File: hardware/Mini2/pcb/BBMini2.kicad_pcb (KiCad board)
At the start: 4 copper layers, 88 x 50 mm, 79 parts, among them J1 Conn_01x02, J2 USB_B_Mini, Q1 MBT2222ADW1T1, SW1 SW_SPDT, SW2 SW_Push, SW3 SW_Push, SW4 SW_Push, U1 ESP8266EX, U2 AT25SF081-SSHF-X, U3 AP2112K-3.3, U4 CP2104, U5 MCP3208, U6 LM2576S-5, U7 HD44780, U8 74HC595, Y1 ABM8-26.000MHZ-10-1-U-T

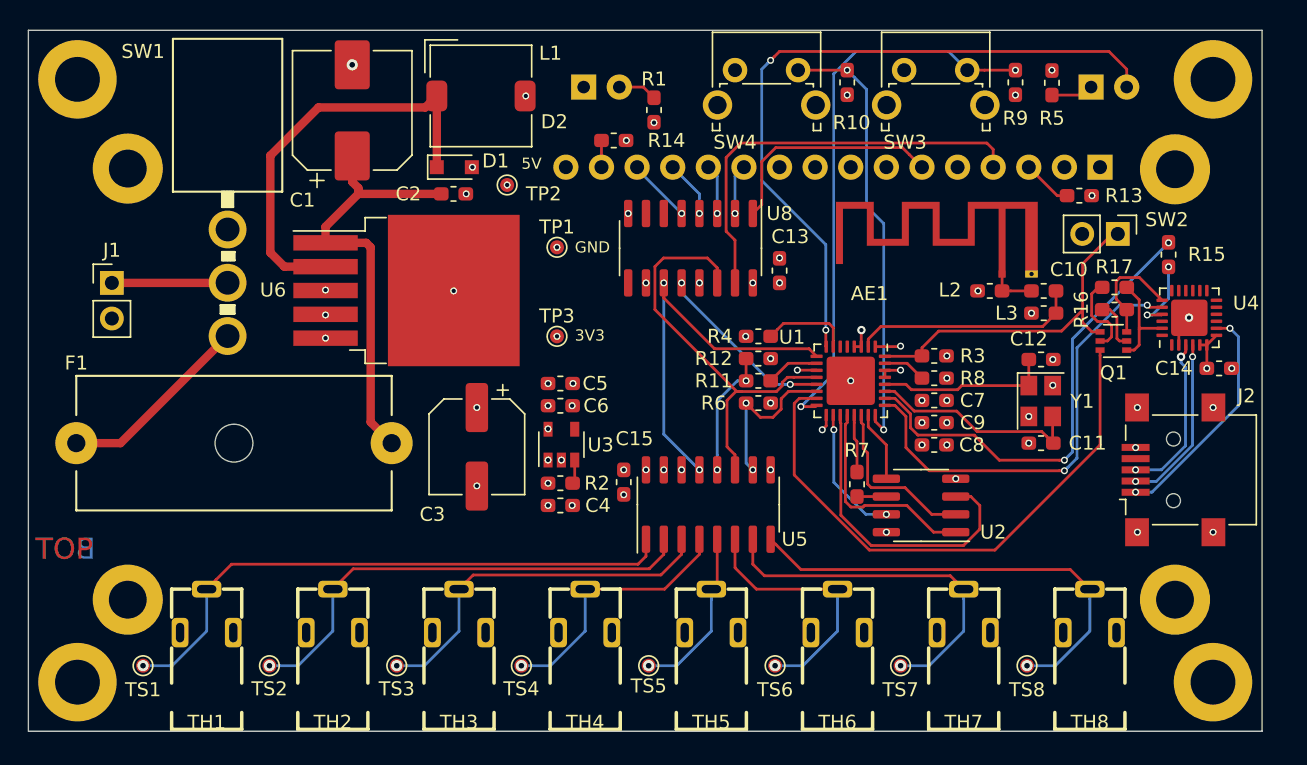
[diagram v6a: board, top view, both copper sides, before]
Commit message: feat: BBMini2 - experimental ESP8266 PCB (SMD)
* implement Case, add 9 V block holder

Issue #23
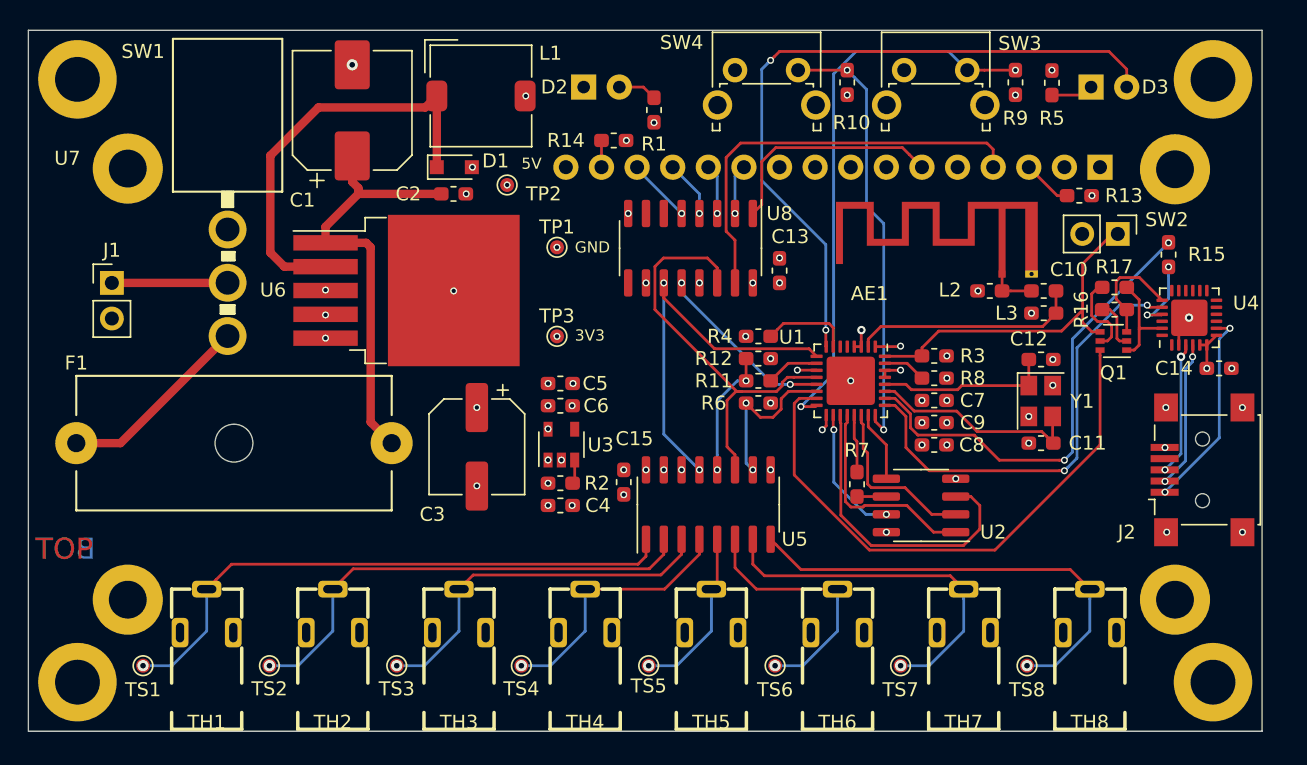
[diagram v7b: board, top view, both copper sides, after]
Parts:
- moved J2 2.07 mm to (98.8, 46.4)
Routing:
- net Net-(J2-Pad3): track 11.7 -> 9.52 mm
- net Net-(J2-Pad1): track 16.6 -> 14.6 mm
- net Net-(J2-Pad2): track 12.3 -> 10.6 mm
